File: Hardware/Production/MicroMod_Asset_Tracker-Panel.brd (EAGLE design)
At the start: 166.6 x 203.5 mm, 1338 parts, among them J11 microSD, J13 TP, J17 NANO_SIM, J18 SARA_USB, J19 NI, J2 JTAG, J20 JTAG, J21 SPI, J24 microSD, J26 MICROMOD-2222-C, J27 !RST!, J28 QWIIC_RIGHT_ANGLE, J32 NANO_SIM, J33 SARA_USB, J34 DIAG, J35 TP, J36 NI, J38 JTAG, J39 SPI, J4 MICROMOD-2222-C, J42 microSD, J44 MICROMOD-2222-C, J45 !RST!, J46 QWIIC_RIGHT_ANGLE, J5 SPI, J50 NANO_SIM, J51 SARA_USB, J52 DIAG, J53 TP, J54 NI, J56 JTAG, J57 SPI, J6 DIAG, J60 microSD, J62 MICROMOD-2222-C, J63 !RST!, J64 QWIIC_RIGHT_ANGLE, J68 NANO_SIM, J69 SARA_USB, J7 QWIIC_RIGHT_ANGLE, J70 DIAG, J71 TP, J72 NI, J9 !RST!, Q1 310mA/60V/1.6Ω, Q10 20V/0.2A/8MHz/1.2Ω/1Vth, Q11 310mA/60V/1.6Ω, Q12 20V/0.2A/8MHz/1.2Ω/1Vth, Q13 20V/4.2A/52mΩ/1.4W, Q14 310mA/60V/1.6Ω, Q15 310mA/60V/1.6Ω, Q16 310mA/60V/1.6Ω, Q17 20V/0.2A/8MHz/1.2Ω/1Vth, Q18 310mA/60V/1.6Ω, Q19 310mA/60V/1.6Ω, Q2 310mA/60V/1.6Ω, Q20 20V/0.2A/8MHz/1.2Ω/1Vth, Q21 20V/4.2A/52mΩ/1.4W, Q22 310mA/60V/1.6Ω, Q23 310mA/60V/1.6Ω, Q24 310mA/60V/1.6Ω, Q25 20V/0.2A/8MHz/1.2Ω/1Vth, Q26 310mA/60V/1.6Ω, Q27 310mA/60V/1.6Ω, Q28 20V/0.2A/8MHz/1.2Ω/1Vth, Q29 20V/4.2A/52mΩ/1.4W, Q3 310mA/60V/1.6Ω, Q30 310mA/60V/1.6Ω, Q31 310mA/60V/1.6Ω, Q32 310mA/60V/1.6Ω, Q4 310mA/60V/1.6Ω, Q5 20V/0.2A/8MHz/1.2Ω/1Vth, Q6 20V/4.2A/52mΩ/1.4W, Q7 310mA/60V/1.6Ω, Q8 20V/0.2A/8MHz/1.2Ω/1Vth, Q9 310mA/60V/1.6Ω, U1 SARA-R5, U10 AP7361C-33FGE, U11 SARA-R5, U12 9DoF IMU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

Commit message: Ready for review
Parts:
- removed JP81, JP82, JP83: JUMPER-SMT_2_NC_TRACE_SILK, SparkFun-Jumpers:SMT-JUMPER_2_NC_TRACE_SILK
- removed JP84: JUMPER-SMT_2_NO_SILK, SparkFun-Jumpers:SMT-JUMPER_2_NO_SILK
- removed U33, U40, U41, U44: TXB0104, SparkFun-IC-Comms:TSSOP14
- removed U34: AP7361C-33FGE, SparkFun-IC-Power:UDFN-8
- removed U35: SARA-R5, SARA_R5:SARA-LGA
- removed U36: 9DoF IMU, SparkFun-Sensors:QFN24-3X3-ICM-20948
- removed U37: 1.8V/100mA, SparkFun-IC-Power:SC70
- removed U38: MCP73831, SparkFun-IC-Power:SOT23-5
- removed U39: 3.3V, SparkFun-IC-Power:SOT23-5
- removed U42: PCA9306, SparkFun-IC-Comms:VSSOP_8PIN
- removed U43: 74HC1G04, SparkFun-IC-Logic:SOT353
- added C117: 47pF, SparkFun-Capacitors:0603
- added C118, C119: 0.1uF, SparkFun-Capacitors:0603
- added C120: 15pF, SparkFun-Capacitors:0603
- added DSR, DSR1, DSR2, DSR3: JUMPER-SMT_3_1-NC_TRACE_SILK, SparkFun-Jumpers:SMT-JUMPER_3_1-NC_TRACE_SILK
- added IC1, IC10, IC11, IC12, IC2, IC3, IC4, IC5, IC6, IC7, IC8, IC9: SN74AVC4T774PW, New_Parts:SOP65P640X120-16N
- added U$525: (no value), output:SIM0
- added U$526, U$527: (no value), output:#SARA_#ON##0
- added U$528: MAX17048, SparkFun-IC-Power:DFN-8
- C100, C36, C64, C70, C71, C93: value 1.0uF -> 0.1uF
- C101: value 4.7uF -> 0.1uF
- C102, C103, C73, C85: value 47pF -> 1.0uF
- C104, C39, C74: value 47pF -> 4.7uF
- C106, C107, C43, C57, C77, C78, C87: value 0.1uF -> 47pF
- C109, C80: value 10uF -> 0.1uF
- C110: value 33pF -> 0.1uF; device New_Parts:0402 -> SparkFun-Capacitors:0603
- C111: value 27pF -> 68pF; device New_Parts:0402 -> SparkFun-Capacitors:0603
- C112: value 1.0uF -> 10uF
- C113: value 0.1uF -> 33pF; device SparkFun-Capacitors:0603 -> New_Parts:0402
- C114: value 47pF -> 27pF; device SparkFun-Capacitors:0603 -> New_Parts:0402
- C115, C55: value 0.1uF -> 1.0uF
- C15: value 47pF -> 68pF
- C24: value 0.22uF -> 15pF
- C25, C61, C68, C91, C98: value 0.1uF -> 0.22uF
- C28, C63, C92: value 10uF -> 0.1uF; device SparkFun-Capacitors:EIA3216 -> SparkFun-Capacitors:0603
- C29: value 1.0uF -> 10uF; device SparkFun-Capacitors:0603 -> SparkFun-Capacitors:EIA3216
- C3: value 1.0uF -> 4.7uF
- C30: value 0.1uF -> 4.7uF
- C32, C59, C88: value 0.22uF -> 0.1uF
- C33: value 1nF -> 0.22uF
- C34, C69: value 0.1uF -> 1nF
- C38, C72: value 4.7uF -> 1.0uF
- C45, C56, C79: value 47pF -> 0.1uF
- C47: value 10uF -> 68pF
- C48: value 33pF -> 10uF; device New_Parts:0402 -> SparkFun-Capacitors:0603
- C49: value 27pF -> 33pF
- C50: value 1.0uF -> 27pF; device SparkFun-Capacitors:0603 -> New_Parts:0402
- C60, C90: value 0.1uF -> 15pF
- C65: value 0.1uF -> 10uF; device SparkFun-Capacitors:0603 -> SparkFun-Capacitors:EIA3216
- C66: value 0.22uF -> 4.7uF
- C67: value 1nF -> 0.1uF
- C81: value 33pF -> 68pF; device New_Parts:0402 -> SparkFun-Capacitors:0603
- C82: value 27pF -> 10uF; device New_Parts:0402 -> SparkFun-Capacitors:0603
- C83: value 1.0uF -> 33pF; device SparkFun-Capacitors:0603 -> New_Parts:0402
- C84: value 0.1uF -> 27pF; device SparkFun-Capacitors:0603 -> New_Parts:0402
- C95: value 0.22uF -> 10uF; device SparkFun-Capacitors:0603 -> SparkFun-Capacitors:EIA3216
- C96: value 1nF -> 4.7uF
- C99: value 1.0uF -> 1nF
- D21, D35, D49: value 3A/10V/280mV -> DT1042-04SO-7; device SparkFun-DiscreteSemi:SOD-323 -> ublox:SOT23-6L
- D22, D36, D50: value DT1042-04SO-7 -> PESD0402; device ublox:SOT23-6L -> New_Parts:0402
- D24, D38, D52: value PESD0402 -> GREEN; device New_Parts:0402 -> SparkFun-LED:LED-0603
- D25, D39, D53: value GREEN -> BLUE
- D26, D40, D54: value BLUE -> 3.3V; device SparkFun-LED:LED-0603 -> SparkFun-DiscreteSemi:SOD-323
- D27, D41, D55: value 3.3V -> WHITE; device SparkFun-DiscreteSemi:SOD-323 -> SparkFun-LED:LED-0603
- D28, D42, D56: value WHITE -> 1A/15V/220mV; device SparkFun-LED:LED-0603 -> SparkFun-DiscreteSemi:DO-214BA
- D7: value 3A/10V/280mV -> 1A/15V/220mV; device SparkFun-DiscreteSemi:SOD-323 -> SparkFun-DiscreteSemi:DO-214BA
- JP23, JP43, JP44, JP64, JP65: value (none) -> JUMPER-SMT_2_NO_SILK; device SparkFun-Jumpers:SMT-JUMPER_3_2-NC_TRACE_SILK -> SparkFun-Jumpers:SMT-JUMPER_2_NO_SILK
- JP26, JP29, JP30, JP46, JP49, JP50, JP51, JP66, JP70, JP71, JP72: value JUMPER-SMT_2_NO_SILK -> JUMPER-SMT_2_NC_TRACE_SILK; device SparkFun-Jumpers:SMT-JUMPER_2_NO_SILK -> SparkFun-Jumpers:SMT-JUMPER_2_NC_TRACE_SILK
- JP27, JP40, JP48, JP60, JP80: value JUMPER-SMT_2_NC_TRACE_SILK -> JUMPER-SMT_2_NO_SILK; device SparkFun-Jumpers:SMT-JUMPER_2_NC_TRACE_SILK -> SparkFun-Jumpers:SMT-JUMPER_2_NO_SILK
- JP41, JP61, JP62: value JUMPER-SMT_2_NC_TRACE_SILK -> (none); device SparkFun-Jumpers:SMT-JUMPER_2_NC_TRACE_SILK -> SparkFun-Jumpers:SMT-JUMPER_3_2-NC_TRACE_SILK
- JP42, JP9: value JUMPER-SMT_2_NO_SILK -> (none); device SparkFun-Jumpers:SMT-JUMPER_2_NO_SILK -> SparkFun-Jumpers:SMT-JUMPER_3_2-NC_TRACE_SILK
- U$132, U$264: value (none) -> MAX17048; device SparkFun-MicroMod:MICROMOD_LOGO_.35 -> SparkFun-IC-Power:DFN-8
- U$134, U$265, U$266, U$397: device output:#CIPO#2 -> SparkFun-MicroMod:MICROMOD_LOGO_.35
- U$136, U$267, U$268, U$399: device output:#COPI#1 -> output:#CIPO#2
- U$138, U$269, U$270, U$401: device output:#GND#4 -> output:#COPI#1
- U$140, U$271, U$272, U$403: device output:#SCK#0 -> output:#GND#4
- U$142, U$273, U$274, U$405: device output:#GND#4 -> output:#SCK#0
- U$144, U$275, U$276, U$407: device output:#A0#5 -> output:#GND#4
- U$146, U$277, U$278, U$409: device output:#A1#4 -> output:#A0#5
- U$148, U$279, U$280, U$411: device output:#D0#1 -> output:#A1#4
- U$150, U$281, U$282, U$413: device output:#D1#0 -> output:#D0#1
- U$152, U$283, U$284, U$415: device output:#PWM0#3 -> output:#D1#0
- U$154, U$285, U$286, U$417: device output:#PWM1#2 -> output:#PWM0#3
- U$156, U$287, U$288, U$419: device output:#3V3#1 -> output:#PWM1#2
- U$158, U$181, U$289, U$290, U$312, U$313, U$421, U$444: device output:#GND#0 -> output:#3V3#1
- U$160, U$183, U$291, U$292, U$314, U$315, U$423, U$446: device output:#SCL#3 -> output:#GND#0
- U$162, U$185, U$293, U$294, U$316, U$317, U$425, U$448: device output:#SDA#2 -> output:#SCL#3
- U$164, U$295: device output:3V37 -> output:#SDA#2
- U$165: device output:BOOT5 -> output:3V37
- U$166: device output:RESET6 -> output:BOOT5
- U$167: device output:VIN8 -> output:RESET6
- U$168: device output:X1 -> output:VIN8
- U$169: device output:Y2 -> output:X1
- U$170, U$321: device output:Z0 -> output:Y2
- U$171: device output:#MEAS#2 -> output:Z0
- U$172: device output:SWD0 -> output:#MEAS#2
- U$173: device output:#BYP#1 -> output:SWD0
- U$174: device output:#RST#1 -> output:#BYP#1
- U$175: device output:#VE#0 -> output:#RST#1
- U$176: device output:#3V3#0 -> output:#VE#0
- U$177: device output:#VIN#1 -> output:#3V3#0
- U$178: device output:MICROSD0 -> output:#VIN#1
- U$179, U$311: device output:#3V3#1 -> output:MICROSD0
- U$187, U$318: device output:#I�C#0 -> output:#SDA#2
- U$188: device output:Y2 -> output:#I�C#0
- U$189: device output:X1 -> output:Y2
- U$190, U$301: device output:Z0 -> output:X1
- U$191, U$323: device output:#GND#4 -> output:Z0
- U$193, U$324, U$325, U$456: device output:#TP#0 -> output:#GND#4
- U$195, U$326, U$327, U$458: device output:#NI#0 -> output:#TP#0
- U$197, U$328, U$329, U$460, U$461: device output:#SARA_USB_D##0 -> output:#NI#0
- U$201, U$332, U$333, U$463, U$464: device output:#SARA_USB_DET#0 -> output:#SARA_USB_D##0
- U$203, U$334, U$335, U$466: device output:#VIN#0 -> output:#SARA_USB_DET#0
- U$205, U$336, U$337, U$468: device output:#3#3V#0 -> output:#VIN#0
- U$207, U$338, U$339, U$470: device output:#VCCIO#0 -> output:#3#3V#0
- U$209, U$340, U$341, U$472: device output:#1#8V#0 -> output:#VCCIO#0
- U$211, U$342: device output:#RST#1 -> output:#1#8V#0
- U$212: device output:#MEAS#2 -> output:#RST#1
- U$213: device output:NI0 -> output:#MEAS#2
- U$214: device output:TP0 -> output:NI0
- U$215, U$347: device output:#USB_D##0 -> output:TP0
- U$217, U$348: device output:#V_USB#0 -> output:#USB_D##0
- U$218: device output:AG0 -> output:#V_USB#0
- U$219: device output:M0 -> output:AG0
- U$220: device output:CHARGE0 -> output:M0
- U$221: device output:ASSET_TRACKER0 -> output:CHARGE0
- U$222: device output:MIC0 -> output:ASSET_TRACKER0
- U$223: device output:#EN#0 -> output:MIC0
- U$224, U$356: device output:#SARA_I�C#0 -> output:#EN#0
- U$226, U$357, U$358, U$489: device output:LTE0 -> output:#SARA_I�C#0
- U$228, U$359, U$360, U$491: device output:GNSS0 -> output:LTE0
- U$230, U$361: device output:#SARA_INT#0 -> output:GNSS0
- U$231: device output:#RI#0 -> output:#SARA_INT#0
- U$232: device output:#DSR#0 -> output:#RI#0
- U$233: device output:#SD_#CS##0 -> output:#DSR#0
- U$234: device output:#IMU_PWR#0 -> output:#SD_#CS##0
- U$235: device output:#LTE_PWR#0 -> output:#IMU_PWR#0
- U$236: device output:#SD_PWR#0 -> output:#LTE_PWR#0
- U$237: device output:#ANT_PWR#0 -> output:#SD_PWR#0
- U$238: device output:#SARA_SCL#0 -> output:#ANT_PWR#0
- U$239: device output:#SARA_SDA#0 -> output:#SARA_SCL#0
- U$240: device output:#CIPO#0 -> output:#SARA_SDA#0
- U$241: device output:22220 -> output:#CIPO#0
- U$242: device output:SARA_ON0 -> output:22220
- U$243: device output:ON0 -> output:SARA_ON0
- U$244: device output:#PDM_CLK#0 -> output:ON0
- U$245: device output:#PDM_DAT#0 -> output:#PDM_CLK#0
- U$246: device output:#DSR#0 -> output:#PDM_DAT#0
- U$247: device output:#G10#0 -> output:#DSR#0
- U$248: device output:#G9#0 -> output:#G10#0
- U$249: device output:#G0#0 -> output:#G9#0
- U$250: device output:#G1#0 -> output:#G0#0
- U$251: device output:#G2#0 -> output:#G1#0
- U$252: device output:#G3#0 -> output:#G2#0
- U$253: device output:#G4#0 -> output:#G3#0
- U$254: device output:#G7#0 -> output:#G4#0
- U$255: device output:#G6#0 -> output:#G7#0
- U$256: device output:#G5#0 -> output:#G6#0
- U$257, U$389: device output:#D0#1 -> output:#G5#0
- U$259, U$390: device output:NANO0 -> output:#D0#1
- U$260: device output:SIM0 -> output:NANO0
- U$261, U$393: device output:#SARA_#ON##0 -> output:SIM0
- U$263, U$394, U$395: device SparkFun-MicroMod:MICROMOD_LOGO_.35 -> output:#SARA_#ON##0
- U$296, U$427: device output:BOOT5 -> output:#SDA#2
- U$297: device output:RESET6 -> output:3V37
- U$298: device output:VIN8 -> output:BOOT5
- U$299: device output:X1 -> output:RESET6
- U$300: device output:Y2 -> output:VIN8
- U$302: device output:#MEAS#2 -> output:Y2
- U$303: device output:SWD0 -> output:Z0
- U$304: device output:#BYP#1 -> output:#MEAS#2
- U$305: device output:#RST#1 -> output:SWD0
- U$306: device output:#VE#0 -> output:#BYP#1
- U$307: device output:#3V3#0 -> output:#RST#1
- U$308: device output:#VIN#1 -> output:#VE#0
- U$309: device output:MICROSD0 -> output:#3V3#0
- U$310, U$442: device output:#3V3#1 -> output:#VIN#1
- U$319, U$450: device output:Y2 -> output:#SDA#2
- U$320: device output:X1 -> output:#I�C#0
- U$322, U$454: device output:#GND#4 -> output:X1
- U$343, U$474: device output:#MEAS#2 -> output:#1#8V#0
- U$344: device output:NI0 -> output:#RST#1
- U$345: device output:TP0 -> output:#MEAS#2
- U$346, U$478: device output:#USB_D##0 -> output:NI0
- U$349, U$480: device output:AG0 -> output:#USB_D##0
- U$350: device output:M0 -> output:#V_USB#0
- U$351: device output:CHARGE0 -> output:AG0
- U$352: device output:ASSET_TRACKER0 -> output:M0
- U$353: device output:MIC0 -> output:CHARGE0
- U$354: device output:#EN#0 -> output:ASSET_TRACKER0
- U$355, U$487: device output:#SARA_I�C#0 -> output:MIC0
- U$362, U$493: device output:#RI#0 -> output:GNSS0
- U$363: device output:#DSR#0 -> output:#SARA_INT#0
- U$364: device output:#SD_#CS##0 -> output:#RI#0
- U$365: device output:#IMU_PWR#0 -> output:#DSR#0
- U$366: device output:#LTE_PWR#0 -> output:#SD_#CS##0
- U$367: device output:#SD_PWR#0 -> output:#IMU_PWR#0
- U$368: device output:#ANT_PWR#0 -> output:#LTE_PWR#0
- U$369: device output:#SARA_SCL#0 -> output:#SD_PWR#0
- U$370: device output:#SARA_SDA#0 -> output:#ANT_PWR#0
- U$371: device output:#CIPO#0 -> output:#SARA_SCL#0
- U$372: device output:22220 -> output:#SARA_SDA#0
- U$373: device output:SARA_ON0 -> output:#CIPO#0
- U$374: device output:ON0 -> output:22220
- U$375: device output:#PDM_CLK#0 -> output:SARA_ON0
- U$376: device output:#PDM_DAT#0 -> output:ON0
- U$377: device output:#DSR#0 -> output:#PDM_CLK#0
- U$378: device output:#G10#0 -> output:#PDM_DAT#0
- U$379: device output:#G9#0 -> output:#DSR#0
- U$380: device output:#G0#0 -> output:#G10#0
- U$381: device output:#G1#0 -> output:#G9#0
- U$382: device output:#G2#0 -> output:#G0#0
- U$383: device output:#G3#0 -> output:#G1#0
- U$384: device output:#G4#0 -> output:#G2#0
- U$385: device output:#G7#0 -> output:#G3#0
- U$386: device output:#G6#0 -> output:#G4#0
- U$387: device output:#G5#0 -> output:#G7#0
- U$388, U$520: device output:#D0#1 -> output:#G6#0
- U$391, U$522: device output:SIM0 -> output:#D0#1
- U$392, U$524: device output:#SARA_#ON##0 -> output:NANO0
- U$396: value (none) -> MAX17048; device output:#CIPO#2 -> SparkFun-IC-Power:DFN-8
- U$398: device output:#COPI#1 -> SparkFun-MicroMod:MICROMOD_LOGO_.35
- U$400: device output:#GND#4 -> output:#CIPO#2
- U$402: device output:#SCK#0 -> output:#COPI#1
- U$406: device output:#A0#5 -> output:#SCK#0
- U$408: device output:#A1#4 -> output:#GND#4
- U$410: device output:#D0#1 -> output:#A0#5
- U$412: device output:#D1#0 -> output:#A1#4
- U$414: device output:#PWM0#3 -> output:#D0#1
- U$416: device output:#PWM1#2 -> output:#D1#0
- U$418: device output:#3V3#1 -> output:#PWM0#3
- U$420: device output:#GND#0 -> output:#PWM1#2
- U$422, U$445: device output:#SCL#3 -> output:#3V3#1
- U$424, U$447: device output:#SDA#2 -> output:#GND#0
- U$426: device output:3V37 -> output:#SCL#3
- U$428: device output:RESET6 -> output:#SDA#2
- U$429: device output:VIN8 -> output:3V37
- U$430: device output:X1 -> output:BOOT5
- U$431: device output:Y2 -> output:RESET6
- U$432: device output:Z0 -> output:VIN8
- U$433: device output:#MEAS#2 -> output:X1
- U$434: device output:SWD0 -> output:Y2
- U$435: device output:#BYP#1 -> output:Z0
- U$436: device output:#RST#1 -> output:#MEAS#2
- U$437: device output:#VE#0 -> output:SWD0
- U$438: device output:#3V3#0 -> output:#BYP#1
- U$439: device output:#VIN#1 -> output:#RST#1
- U$440: device output:MICROSD0 -> output:#VE#0
- U$441: device output:#3V3#1 -> output:#3V3#0
- U$443: device output:#GND#0 -> output:MICROSD0
- U$449: device output:#I�C#0 -> output:#SCL#3
- U$451: device output:X1 -> output:#SDA#2
- U$452: device output:Z0 -> output:#I�C#0
- U$453: device output:#GND#4 -> output:Y2
- U$455: device output:#TP#0 -> output:Z0
- U$457: device output:#NI#0 -> output:#GND#4
- U$459: device output:#SARA_USB_D##0 -> output:#TP#0
- U$465: device output:#VIN#0 -> output:#SARA_USB_D##0
- U$467: device output:#3#3V#0 -> output:#SARA_USB_DET#0
- U$469: device output:#VCCIO#0 -> output:#VIN#0
- U$471: device output:#1#8V#0 -> output:#3#3V#0
- U$473: device output:#RST#1 -> output:#VCCIO#0
- U$475: device output:NI0 -> output:#1#8V#0
- U$476: device output:TP0 -> output:#RST#1
- U$477: device output:#USB_D##0 -> output:#MEAS#2
- U$479: device output:#V_USB#0 -> output:TP0
- U$481: device output:M0 -> output:#USB_D##0
- U$482: device output:CHARGE0 -> output:#V_USB#0
- U$483: device output:ASSET_TRACKER0 -> output:AG0
- U$484: device output:MIC0 -> output:M0
- U$485: device output:#EN#0 -> output:CHARGE0
- U$486: device output:#SARA_I�C#0 -> output:ASSET_TRACKER0
- U$488: device output:LTE0 -> output:#EN#0
- U$490: device output:GNSS0 -> output:#SARA_I�C#0
- U$492: device output:#SARA_INT#0 -> output:LTE0
- U$494: device output:#DSR#0 -> output:GNSS0
- U$495: device output:#SD_#CS##0 -> output:#SARA_INT#0
- U$496: device output:#IMU_PWR#0 -> output:#RI#0
- U$497: device output:#LTE_PWR#0 -> output:#DSR#0
- U$498: device output:#SD_PWR#0 -> output:#SD_#CS##0
- U$499: device output:#ANT_PWR#0 -> output:#IMU_PWR#0
- U$500: device output:#SARA_SCL#0 -> output:#LTE_PWR#0
- U$501: device output:#SARA_SDA#0 -> output:#SD_PWR#0
- U$502: device output:#CIPO#0 -> output:#ANT_PWR#0
- U$503: device output:22220 -> output:#SARA_SCL#0
- U$504: device output:SARA_ON0 -> output:#SARA_SDA#0
- U$505: device output:ON0 -> output:#CIPO#0
- U$506: device output:#PDM_CLK#0 -> output:22220
- U$507: device output:#PDM_DAT#0 -> output:SARA_ON0
- U$508: device output:#DSR#0 -> output:ON0
- U$509: device output:#G10#0 -> output:#PDM_CLK#0
- U$510: device output:#G9#0 -> output:#PDM_DAT#0
- U$511: device output:#G0#0 -> output:#DSR#0
- U$512: device output:#G1#0 -> output:#G10#0
- U$513: device output:#G2#0 -> output:#G9#0
- U$514: device output:#G3#0 -> output:#G0#0
- U$515: device output:#G4#0 -> output:#G1#0
- U$516: device output:#G7#0 -> output:#G2#0
- U$517: device output:#G6#0 -> output:#G3#0
- U$518: device output:#G5#0 -> output:#G4#0
- U$519: device output:#D0#1 -> output:#G7#0
- U$521: device output:NANO0 -> output:#G5#0
- U$523: device output:#SARA_#ON##0 -> output:#D0#1
- U10: value AP7361C-33FGE -> 1.8V/100mA; device SparkFun-IC-Power:UDFN-8 -> SparkFun-IC-Power:SC70
- U11: value SARA-R5 -> MCP73831; device SARA_R5:SARA-LGA -> SparkFun-IC-Power:SOT23-5
- U12: value 9DoF IMU -> 3.3V; device SparkFun-Sensors:QFN24-3X3-ICM-20948 -> SparkFun-IC-Power:SOT23-5
- U15: value 1.8V/100mA -> PCA9306; device SparkFun-IC-Power:SC70 -> SparkFun-IC-Comms:VSSOP_8PIN
- U16: value MCP73831 -> 74HC1G04; device SparkFun-IC-Power:SOT23-5 -> SparkFun-IC-Logic:SOT353
- U17: value 3.3V -> AP7361C-33FGE; device SparkFun-IC-Power:SOT23-5 -> SparkFun-IC-Power:UDFN-8
- U18, U6: value TXB0104 -> SARA-R5; device SparkFun-IC-Comms:TSSOP14 -> SARA_R5:SARA-LGA
- U19, U9: value TXB0104 -> 9DoF IMU; device SparkFun-IC-Comms:TSSOP14 -> SparkFun-Sensors:QFN24-3X3-ICM-20948
- U20: value PCA9306 -> 1.8V/100mA; device SparkFun-IC-Comms:VSSOP_8PIN -> SparkFun-IC-Power:SC70
- U21: value 74HC1G04 -> MCP73831; device SparkFun-IC-Logic:SOT353 -> SparkFun-IC-Power:SOT23-5
- U22, U30: value TXB0104 -> 3.3V; device SparkFun-IC-Comms:TSSOP14 -> SparkFun-IC-Power:SOT23-5
- U23: value AP7361C-33FGE -> PCA9306; device SparkFun-IC-Power:UDFN-8 -> SparkFun-IC-Comms:VSSOP_8PIN
- U24: value SARA-R5 -> 74HC1G04; device SARA_R5:SARA-LGA -> SparkFun-IC-Logic:SOT353
- U25: value 9DoF IMU -> AP7361C-33FGE; device SparkFun-Sensors:QFN24-3X3-ICM-20948 -> SparkFun-IC-Power:UDFN-8
- U26: value 1.8V/100mA -> SARA-R5; device SparkFun-IC-Power:SC70 -> SARA_R5:SARA-LGA
- U27: value MCP73831 -> 9DoF IMU; device SparkFun-IC-Power:SOT23-5 -> SparkFun-Sensors:QFN24-3X3-ICM-20948
- U28: value 3.3V -> 1.8V/100mA; device SparkFun-IC-Power:SOT23-5 -> SparkFun-IC-Power:SC70
- U29: value TXB0104 -> MCP73831; device SparkFun-IC-Comms:TSSOP14 -> SparkFun-IC-Power:SOT23-5
- U4: value TXB0104 -> AP7361C-33FGE; device SparkFun-IC-Comms:TSSOP14 -> SparkFun-IC-Power:UDFN-8
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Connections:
- removed net N$119 (its old number): JP51.2, R130.1
- removed net N$160 (its old number): JP72.2, R175.1
- removed net N$18 (its old number): JP9.2, R20.1
- removed net N$78 (its old number): JP30.2, R85.1
- new net N$120: J44.52, JP58.1
- new net N$161: J62.52, JP78.1
- new net N$23: DSR.2, IC2.8
- new net N$79: J26.52, JP38.1
- net !RESET!1: now also C34.1, U16.2; no longer C33.1, U21.2
- net !RESET!2: now also C69.1, U24.2; no longer C67.1, U32.2
- net !RESET!3: now also C99.1, U32.2; no longer C96.1, U43.2
- net 1.8V: now also IC3.1, IC3.16; no longer U9.1, U9.8
- net 1.8V1: now also C37.1, IC6.1, IC6.16, U10.5, U9.13, U9.8; no longer C35.1, U12.13, U12.8, U15.5, U22.1, U22.8
- net 1.8V2: now also C71.1, C72.1, IC9.1, IC9.16, U19.13, U19.8, U20.5; no longer C69.1, C70.1, U25.13, U25.8, U26.5, U33.1, U33.8
- net 1.8V3: now also C101.1, C102.1, IC12.1, IC12.16, U27.13, U27.8, U28.5; no longer C98.1, C99.1, U36.13, U36.8, U37.5, U44.1, U44.8
- net 3.3V: now also C24.1, IC1.15, IC2.15, IC3.15; no longer U4.14, U6.14, U9.14
- net 3.3V1: now also C26.1, C38.1, C48.1, C60.1, D24.A, D27.A, IC4.15, IC5.15, IC6.15, JP26.2, JP9.2, U10.1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; no longer C25.1, C37.1, C44.1, D26.A, D28.A, JP23.2, JP27.2, U11.51, U11.52, U11.53, U15.1, U18.14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
- net 3.3V2: now also C62.1, C73.1, C81.1, C82.1, C90.1, D38.A, D41.A, IC7.15, IC8.15, IC9.15, JP41.2, JP42.2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; no longer C60.1, C71.1, C78.1, C79.1, D40.A, D42.A, JP43.2, JP44.2, JP48.2, U24.51, U24.52, U24.53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
- net 3.3V3: now also C103.1, C110.1, C111.1, C112.1, C120.1, C92.1, D52.A, D55.A, IC10.15, IC11.15, IC12.15, JP61.2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; no longer C100.1, C107.1, C108.1, C109.1, C89.1, D54.A, D56.A, JP64.2, JP65.2, JP69.2, U35.51, U35.52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
- net ANT_GNSS_PWR_EN1: now also D26.C, JP35.2, U12.3; no longer D27.C, JP37.2, U17.3
- net ANT_GNSS_PWR_EN2: now also D40.C, JP55.2, U22.3; no longer D41.C, JP58.2, U28.3
- net ANT_GNSS_PWR_EN3: now also D54.C, JP75.2, U30.3; no longer D55.C, JP79.2, U39.3
- net CHG_LED1: now also U11.1; no longer U16.1
- net CHG_LED2: now also U21.1; no longer U27.1
- net CHG_LED3: now also U29.1; no longer U38.1
- net CTS1: now also IC1.12; no longer U4.11
- net CTS2: now also IC4.12; no longer U18.11
- net CTS3: now also IC7.12; no longer U29.11
- net CTS4: now also IC10.12; no longer U40.11
- net DCD: now also IC2.13; no longer U6.12
- net DCD1: now also IC5.13; no longer U19.12
- net DCD2: now also IC8.13; no longer U30.12
- net DCD3: now also IC11.13; no longer U41.12
- net DSR: now also IC2.11; no longer U6.10
- net DSR1: now also IC5.11, JP36.2; no longer JP38.2, U19.10
- net DSR2: now also IC8.11, JP56.2; no longer JP59.2, U30.10
- net DSR3: now also IC11.11, JP76.2; no longer JP80.2, U41.10
- net DTR: now also IC2.14; no longer U6.13
- net DTR1: now also IC5.14; no longer U19.13
- net DTR2: now also IC8.14; no longer U30.13
- net DTR3: now also IC11.14; no longer U41.13
- net G11: now also JP30.1; no longer JP32.1
- net G12: now also JP31.1; no longer JP33.1
- net G13: now also JP32.1; no longer JP34.1
- net G14: now also JP33.1; no longer JP35.1
- net G15: now also JP34.1; no longer JP36.1
- net G16: now also JP35.1; no longer JP37.1
- net G17: now also JP36.1; no longer JP38.1
- net G18: now also JP39.1; no longer JP41.1
- net G19: now also JP40.1; no longer JP42.1
- net G20: now also JP49.1; no longer JP52.1
- net G21: now also JP50.1; no longer JP53.1
- net G22: now also JP51.1; no longer JP54.1
- net G23: now also JP52.1; no longer JP55.1
- net G24: now also JP53.1; no longer JP56.1
- net G25: now also JP54.1; no longer JP57.1
- net G26: now also JP55.1; no longer JP58.1
- net G27: now also JP56.1; no longer JP59.1
- net G28: now also JP59.1; no longer JP62.1
- net G29: now also JP60.1; no longer JP63.1
- net G30: now also JP69.1; no longer JP73.1
- net G31: now also JP70.1; no longer JP74.1
- net G32: now also JP71.1; no longer JP75.1
- net G33: now also JP72.1; no longer JP76.1
- net G34: now also JP73.1; no longer JP77.1
- net G35: now also JP74.1; no longer JP78.1
- net G36: now also JP75.1; no longer JP79.1
- net G37: now also JP76.1; no longer JP80.1
- net G38: now also JP79.1; no longer JP83.1
- net G39: now also JP80.1; no longer JP84.1
- net G8: now also JP29.1; no longer JP31.1
- net GND: now also C24.2, DSR.1, IC1.10, IC1.2, IC1.8, IC1.9, IC2.1, IC2.10, IC2.9, IC3.10, IC3.2, IC3.7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; no longer JP9.1, U4.7, U6.7, U9.7
- net GND1: now also C28.2, C29.-, C41.2, C44.1, C48.2, C59.2, C60.2, D21.2, D21.5, D26.A, DSR1.1, IC4.10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; no longer C24.2, C28.-, C29.2, C41.1, C44.2, C49.2, D22.5, D24.2, D27.A, JP30.1, U10.4, U10.EP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
- net GND2: now also C63.2, C65.-, C75.2, C76.2, C78.1, C79.1, C81.2, C88.2, C89.2, C90.2, D35.2, D35.5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; no longer C59.2, C60.2, C63.-, C65.2, C75.1, C76.1, C78.2, C79.2, C83.2, D36.5, D38.2, D41.A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
- net GND3: now also C104.2, C105.2, C106.2, C107.1, C108.1, C109.1, C110.2, C117.2, C118.2, C119.2, C120.2, C92.2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; no longer C104.1, C105.1, C106.1, C107.2, C108.2, C109.2, C113.2, C88.2, C89.2, C90.2, C92.-, C95.2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
- net I2C_SCL: now also U$132.P$7
- net I2C_SCL1: now also U$264.P$7
- net I2C_SCL2: now also U$396.P$7
- net I2C_SCL3: now also U$528.P$7
- net I2C_SDA: now also U$132.P$8
- net I2C_SDA1: now also U$264.P$8
- net I2C_SDA2: now also U$396.P$8
- net I2C_SDA3: now also U$528.P$8
- net I2S_SCK/PDM_CLK1: now also JP37.2; no longer JP39.2
- net I2S_SCK/PDM_CLK2: now also JP57.2; no longer JP60.2
- net I2S_SCK/PDM_CLK3: now also JP77.2; no longer JP81.2
- net I2S_WS/PDM_DAT1: now also JP38.2; no longer JP40.2
- net I2S_WS/PDM_DAT2: now also JP58.2; no longer JP61.2
- net I2S_WS/PDM_DAT3: now also JP78.2; no longer JP82.2
- net ICM-20948-LV_!CS!: now also IC3.6; no longer U9.5
- net ICM-20948-LV_!CS!1: now also IC6.6, U9.22; no longer U12.22, U22.5
- net ICM-20948-LV_!CS!2: now also IC9.6, U19.22; no longer U25.22, U33.5
- net ICM-20948-LV_!CS!3: now also IC12.6, U27.22; no longer U36.22, U44.5
- net ICM-20948-LV_INT: now also IC3.3; no longer U9.2
- net ICM-20948-LV_INT1: now also IC6.3, U9.12; no longer U12.12, U22.2
- net ICM-20948-LV_INT2: now also IC9.3, U19.12; no longer U25.12, U33.2
- net ICM-20948-LV_INT3: now also IC12.3, U27.12; no longer U36.12, U44.2
- net ICM-20948-LV_SCK: now also IC3.5; no longer U9.4
- net ICM-20948-LV_SCK1: now also IC6.5, U9.23; no longer U12.23, U22.4
- net ICM-20948-LV_SCK2: now also IC9.5, U19.23; no longer U25.23, U33.4
- net ICM-20948-LV_SCK3: now also IC12.5, U27.23; no longer U36.23, U44.4
- net ICM-20948-LV_SDI: now also IC3.4; no longer U9.3
- net ICM-20948-LV_SDI1: now also IC6.4, U9.24; no longer U12.24, U22.3
- net ICM-20948-LV_SDI2: now also IC9.4, U19.24; no longer U25.24, U33.3
- net ICM-20948-LV_SDI3: now also IC12.4, U27.24; no longer U36.24, U44.3
- net ICM-20948-LV_SDO1: now also U9.9; no longer U12.9
- net ICM-20948-LV_SDO2: now also U19.9; no longer U25.9
- net ICM-20948-LV_SDO3: now also U27.9; no longer U36.9
- net ICM_!CS!: now also IC3.11; no longer U9.10
- net ICM_!CS!1: now also IC6.11; no longer U22.10
- net ICM_!CS!2: now also IC9.11; no longer U33.10
- net ICM_!CS!3: now also IC12.11; no longer U44.10
- net ICM_INT: now also IC3.14; no longer U9.13
- net ICM_INT1: now also IC6.14; no longer U22.13
- net ICM_INT2: now also IC9.14; no longer U33.13
- net ICM_INT3: now also IC12.14; no longer U44.13
- net ICM_PWR1: now also JP32.2, U10.3; no longer JP34.2, U15.3
- net ICM_PWR2: now also JP52.2, U20.3; no longer JP55.2, U26.3
- net ICM_PWR3: now also JP72.2, U28.3; no longer JP76.2, U37.3
- net LTE_PWR_ON1: now also JP31.2; no longer JP33.2
- net LTE_PWR_ON2: now also JP51.2; no longer JP54.2
- net LTE_PWR_ON3: now also JP71.2; no longer JP75.2
- net MICROSD_PWR1: now also JP30.2; no longer JP32.2
- net MICROSD_PWR2: now also JP50.2; no longer JP53.2
- net MICROSD_PWR3: now also JP70.2; no longer JP74.2
- net N$100: now also C84.1, D36.1; no longer C82.1, D37.1
- net N$101: now also C85.1, C86.1, U22.5; no longer C83.1, C84.1, U28.5
- net N$102: now also C87.1; no longer C85.1
- net N$103: now also U23.P7, U23.P8; no longer U31.P7, U31.P8
- net N$106: now also U24.4; no longer U32.4
- net N$107: now also JP46.1; no longer JP48.1
- net N$108: now also U18.4; no longer U24.4
- net N$111: now also D38.C; no longer D39.C
- net N$114: now also D39.C; no longer D40.C
- net N$115: now also U18.13; no longer U24.13
- net N$116: now also U18.12; no longer U24.12
- net N$117: now also JP47.2; no longer JP49.2
- net N$118: now also JP48.2; no longer JP50.2
- net N$121: now also J44.50, JP57.1; no longer J44.52, JP61.1
- net N$122: now also D41.C, R134.2; no longer J44.50, JP60.1
- net N$123: now also DSR2.2, IC8.8; no longer D42.C, R134.2
- net N$127: now also JP61.3; no longer JP64.3
- net N$128: now also JP61.1; no longer JP64.1
- net N$134: now also U25.5; no longer U34.5
- net N$135: now also JP62.3; no longer JP65.3
- net N$136: now also JP62.1; no longer JP65.1
- net N$137: now also C100.1, U27.10; no longer C97.1, U36.10
- net N$138: now also U29.5; no longer U38.5
- net N$140: now also C113.2; no longer C110.2
- net N$141: now also C114.1, D50.1; no longer C111.1, D51.1
- net N$142: now also C115.1, C116.1, U30.5; no longer C112.1, C113.1, U39.5
- net N$143: now also C117.1; no longer C114.1
- net N$144: now also U31.P7, U31.P8; no longer U42.P7, U42.P8
- net N$147: now also U32.4; no longer U43.4
- net N$148: now also JP66.1; no longer JP69.1
- net N$149: now also U26.4; no longer U35.4
- net N$152: now also D52.C; no longer D53.C
- net N$155: now also D53.C; no longer D54.C
- net N$156: now also U26.13; no longer U35.13
- net N$157: now also U26.12; no longer U35.12
- net N$158: now also JP67.2; no longer JP70.2
- net N$159: now also JP68.2; no longer JP71.2
- net N$162: now also J62.50, JP77.1; no longer J62.52, JP82.1
- net N$163: now also D55.C, R179.2; no longer J62.50, JP81.1
- net N$164: now also DSR3.2, IC11.8; no longer D56.C, R179.2
- net N$41: now also JP9.3; no longer JP22.3
- net N$42: now also JP9.1; no longer JP22.1
- net N$50: now also U4.5; no longer U10.5
- net N$53: now also JP22.3; no longer JP23.3
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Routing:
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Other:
- board size 166.6 x 203.5 mm -> 166.6 x 199.6 mm

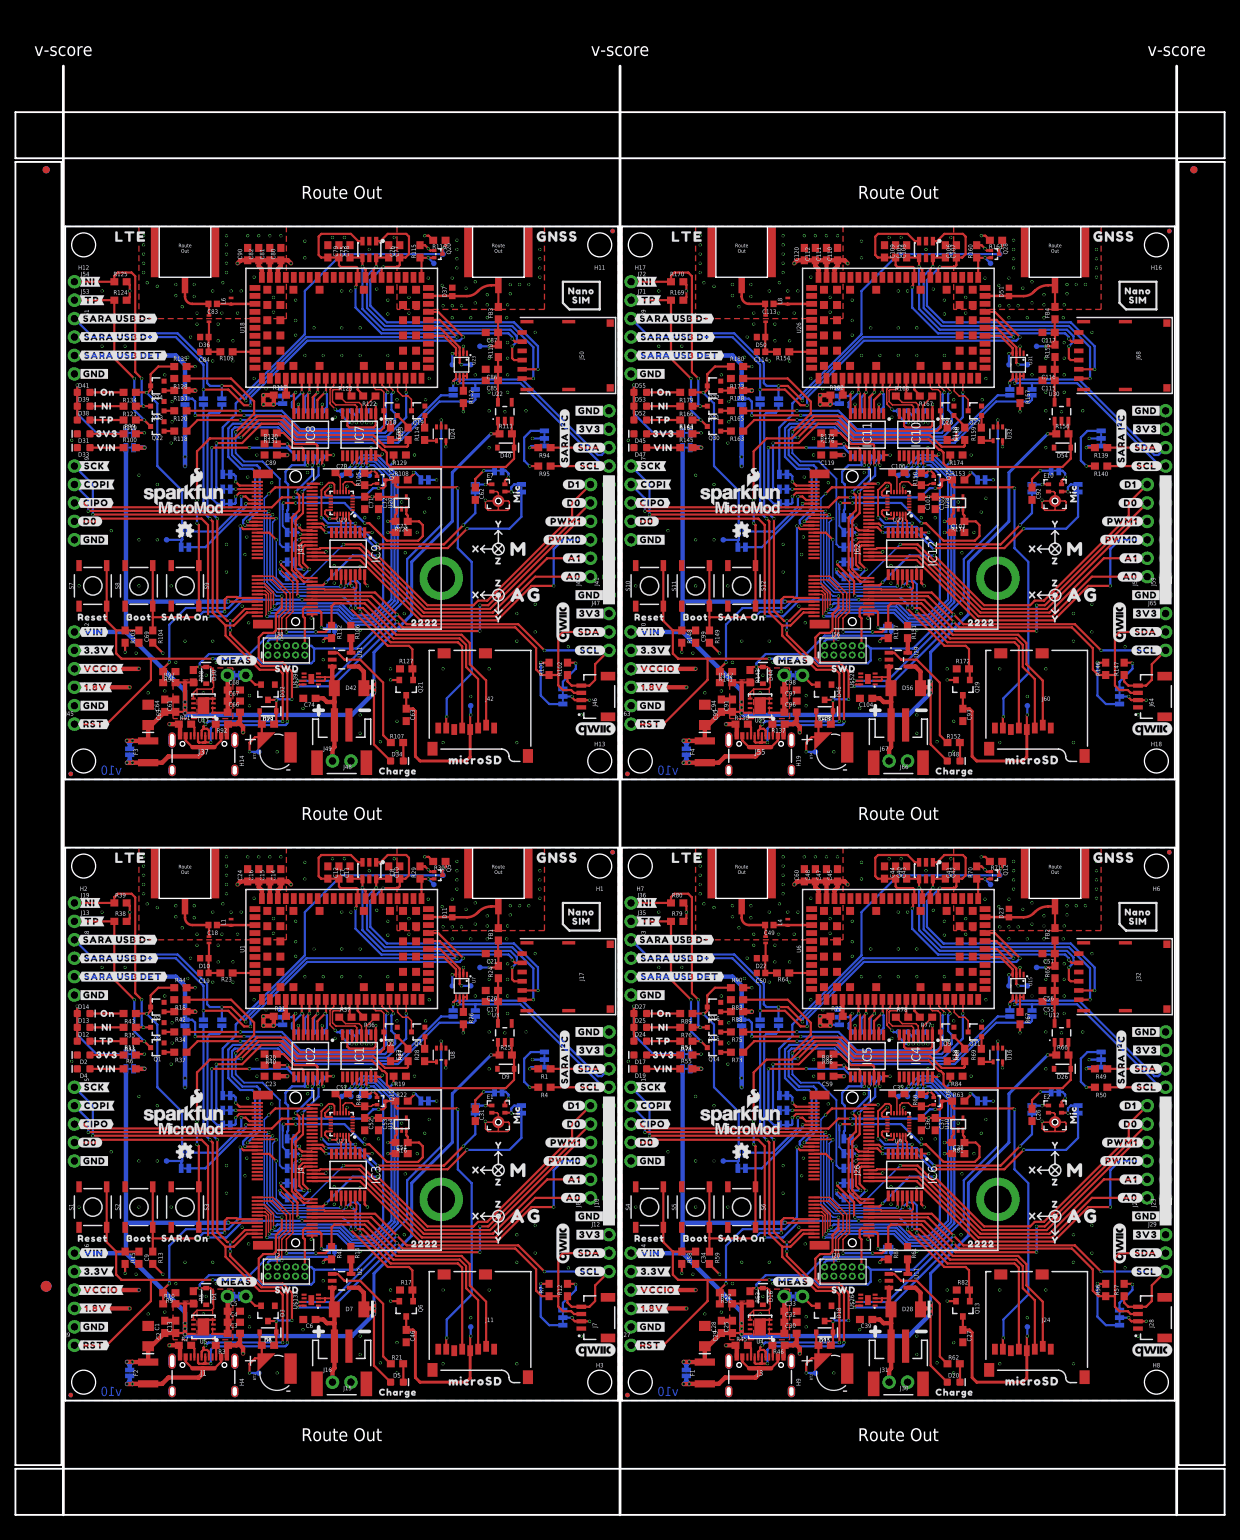
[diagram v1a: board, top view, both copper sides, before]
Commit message: Rerun panelizer to get correct panel size.
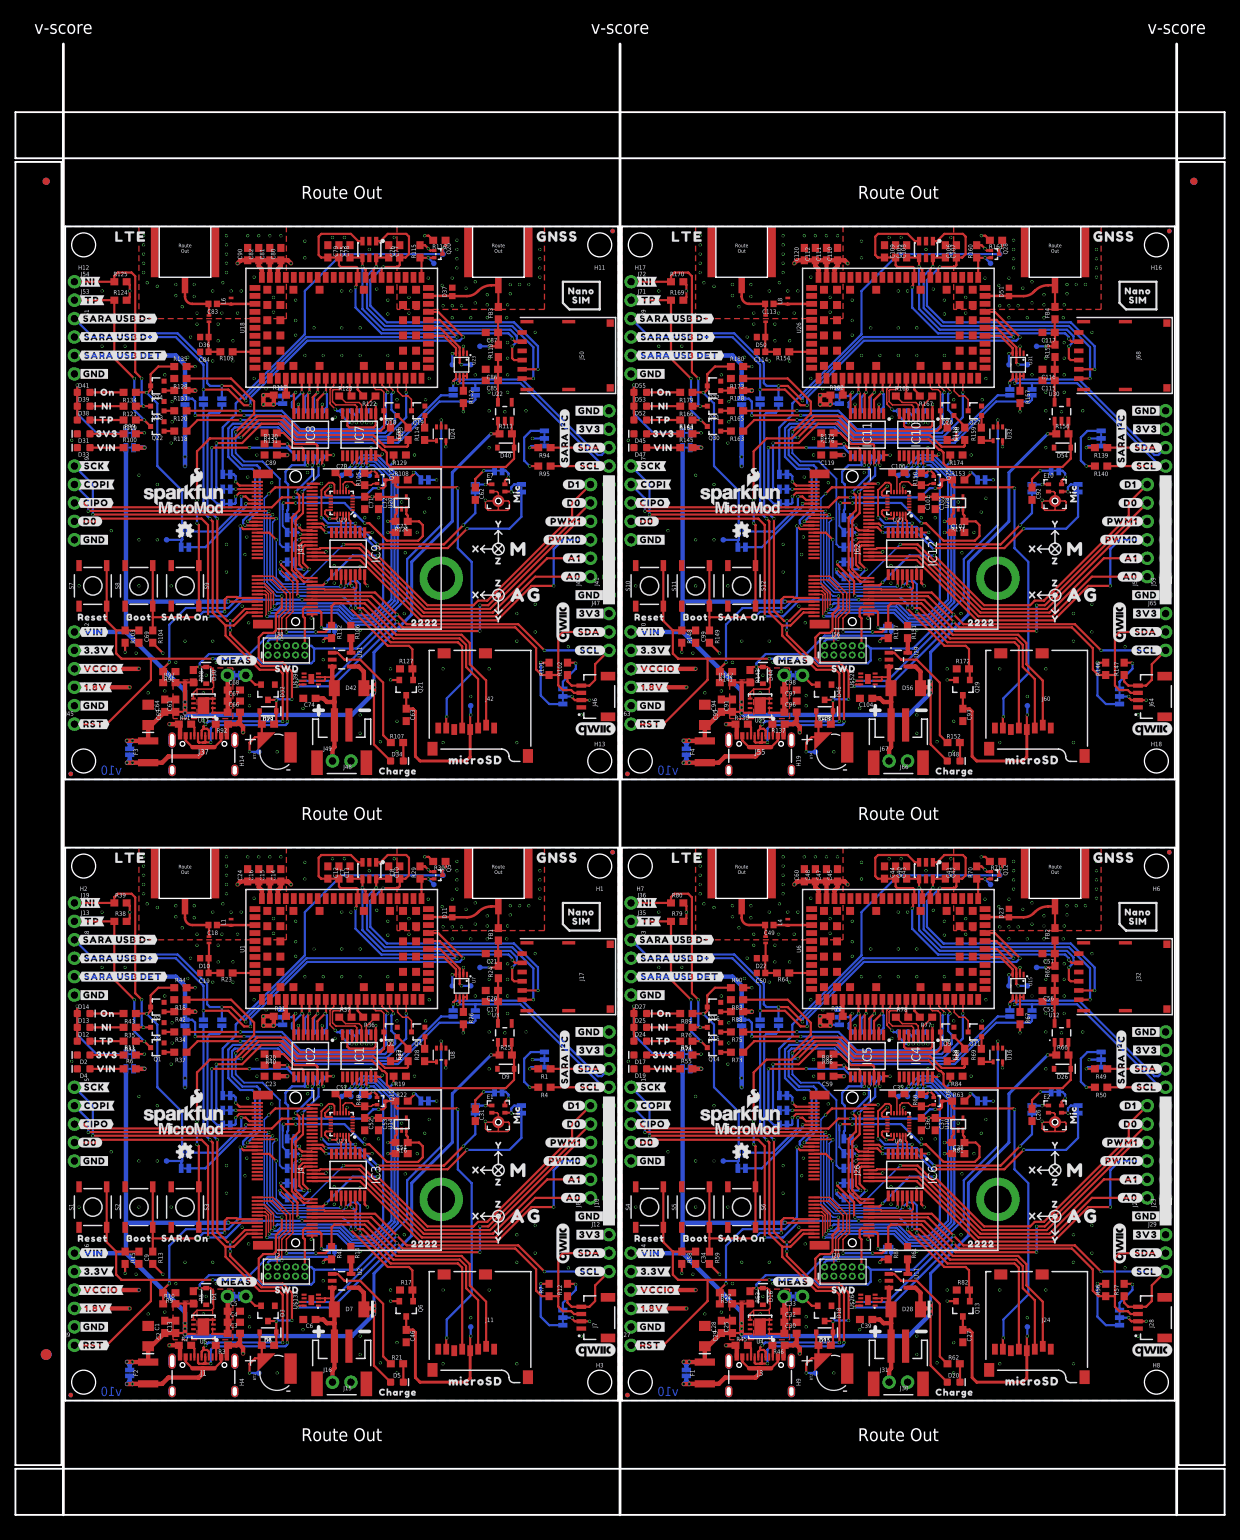
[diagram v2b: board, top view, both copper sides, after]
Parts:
- moved E$5 9.40 mm to (-2.62, 6.35)
- moved E$6 9.40 mm to (-2.62, 6.35)
- moved E$1 1.59 mm to (-2.62, 168.0)
- moved E$2 1.59 mm to (-2.62, 168.0)
- moved E$3 1.59 mm to (155.5, 168.0)
- moved E$4 1.59 mm to (155.5, 168.0)
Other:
- board size 166.6 x 199.6 mm -> 166.6 x 202.7 mm
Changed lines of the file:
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@@
 <?xml version="1.0" encoding="utf-8"?>
 <!DOCTYPE eagle SYSTEM "eagle.dtd">
-<eagle version="9.6.0">
+<eagle version="9.6.2">
 <drawing>
 <settings>
@@
 <text x="114.808" y="80.899" size="1.778" layer="20" font="vector" ratio="15" align="center">Route Out</text>
 <text x="114.808" y="166.497" size="1.778" layer="20" font="vector" ratio="15" align="center">Route Out</text>
-<wire x1="-0.254" y1="-15.748" x2="-0.254" y2="183.896" width="0.381" layer="46"/>
-<text x="-0.254" y="186.182" size="1.778" layer="46" font="vector" ratio="15" align="center">v-score</text>
-<wire x1="76.454" y1="-15.748" x2="76.454" y2="183.896" width="0.381" layer="46"/>
-<text x="76.454" y="186.182" size="1.778" layer="46" font="vector" ratio="15" align="center">v-score</text>
-<wire x1="153.162" y1="-15.748" x2="153.162" y2="183.896" width="0.381" layer="46"/>
-<text x="153.162" y="186.182" size="1.778" layer="46" font="vector" ratio="15" align="center">v-score</text>
+<wire x1="-0.254" y1="-15.748" x2="-0.254" y2="186.944" width="0.381" layer="46"/>
+<text x="-0.254" y="189.23" size="1.778" layer="46" font="vector" ratio="15" align="center">v-score</text>
+<wire x1="76.454" y1="-15.748" x2="76.454" y2="186.944" width="0.381" layer="46"/>
+<text x="76.454" y="189.23" size="1.778" layer="46" font="vector" ratio="15" align="center">v-score</text>
+<wire x1="153.162" y1="-15.748" x2="153.162" y2="186.944" width="0.381" layer="46"/>
+<text x="153.162" y="189.23" size="1.778" layer="46" font="vector" ratio="15" align="center">v-score</text>
 <wire x1="-6.858" y1="-9.398" x2="159.766" y2="-9.398" width="0.254" layer="20"/>
 <wire x1="159.766" y1="-9.398" x2="159.766" y2="-15.748" width="0.254" layer="20"/>
@@
 <attribute name="VALUE" x="113.157" y="99.441" size="0.6096" layer="27" font="vector" ratio="20" rot="R90" align="bottom-center"/>
 </element>
-<element name="E$1" library="SparkFun-Aesthetics" package="FIDUCIAL-1X2" value="" x="-2.62381875" y="169.6085" smashed="yes"/>
-<element name="E$2" library="SparkFun-Aesthetics" package="FIDUCIAL-1X2" value="" x="-2.62381875" y="169.6085" smashed="yes" rot="MR0"/>
-<element name="E$3" library="SparkFun-Aesthetics" package="FIDUCIAL-1X2" value="" x="155.53181875" y="169.6085" smashed="yes"/>
-<element name="E$4" library="SparkFun-Aesthetics" package="FIDUCIAL-1X2" value="" x="155.53181875" y="169.6085" smashed="yes" rot="MR0"/>
-<element name="E$5" library="SparkFun-Retired" package="FIDUCIAL-1.5X3" value="" x="-2.62381875" y="15.748" smashed="yes"/>
-<element name="E$6" library="SparkFun-Retired" package="FIDUCIAL-1.5X3" value="" x="-2.62381875" y="15.748" smashed="yes" rot="MR0"/>
+<element name="E$1" library="SparkFun-Aesthetics" package="FIDUCIAL-1X2" value="" x="-2.62381875" y="168.021" smashed="yes"/>
+<element name="E$2" library="SparkFun-Aesthetics" package="FIDUCIAL-1X2" value="" x="-2.62381875" y="168.021" smashed="yes" rot="MR0"/>
+<element name="E$3" library="SparkFun-Aesthetics" package="FIDUCIAL-1X2" value="" x="155.53181875" y="168.021" smashed="yes"/>
+<element name="E$4" library="SparkFun-Aesthetics" package="FIDUCIAL-1X2" value="" x="155.53181875" y="168.021" smashed="yes" rot="MR0"/>
+<element name="E$5" library="SparkFun-Retired" package="FIDUCIAL-1.5X3" value="" x="-2.62381875" y="6.35" smashed="yes"/>
+<element name="E$6" library="SparkFun-Retired" package="FIDUCIAL-1.5X3" value="" x="-2.62381875" y="6.35" smashed="yes" rot="MR0"/>
 </elements>
 <signals>
